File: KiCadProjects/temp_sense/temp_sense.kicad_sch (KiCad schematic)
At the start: 16 parts, among them J1 Screw_Terminal_01x02, J2 Conn_01x03_Pin, J3 Conn_01x02_Pin, U1 ADS1115IDGS, U2 INA827AIDGKR

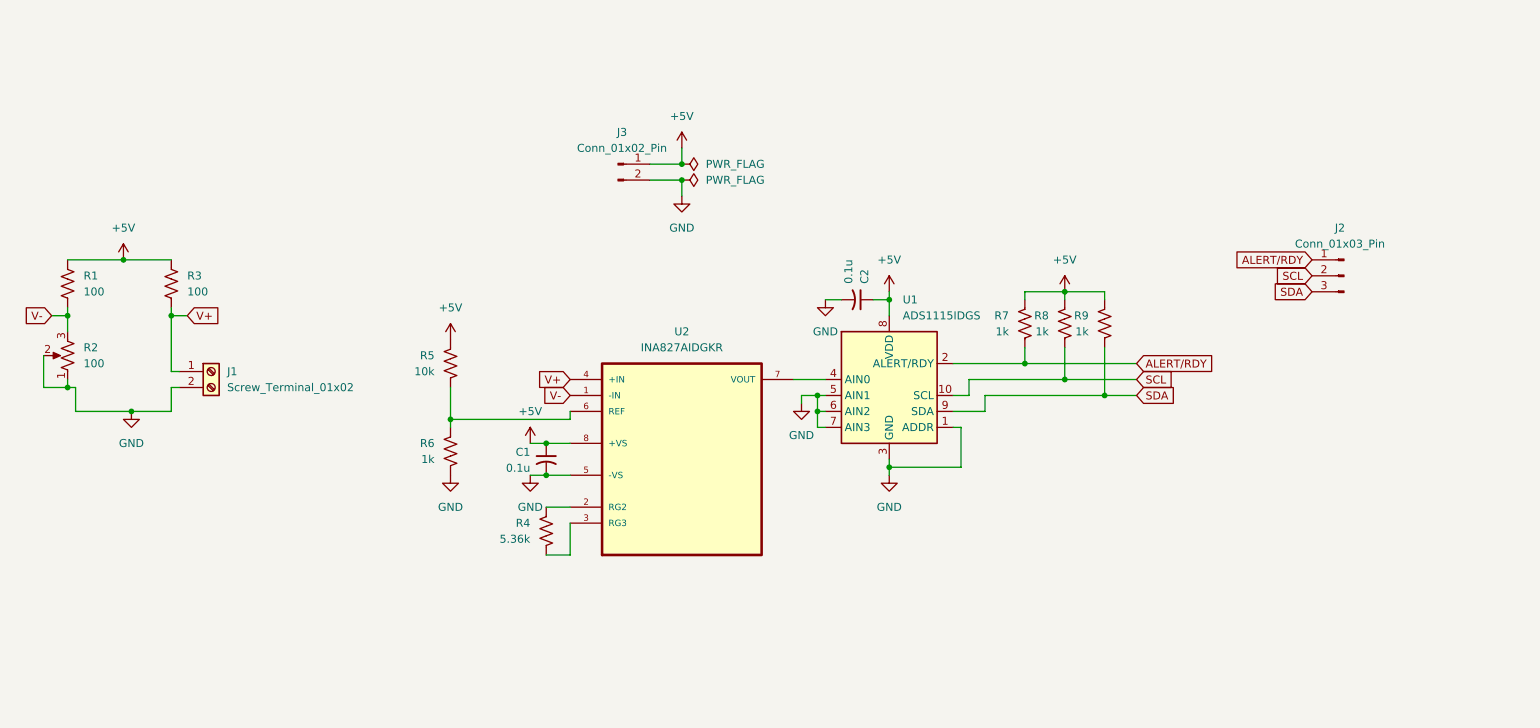
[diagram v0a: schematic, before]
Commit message: updates to temp circuit
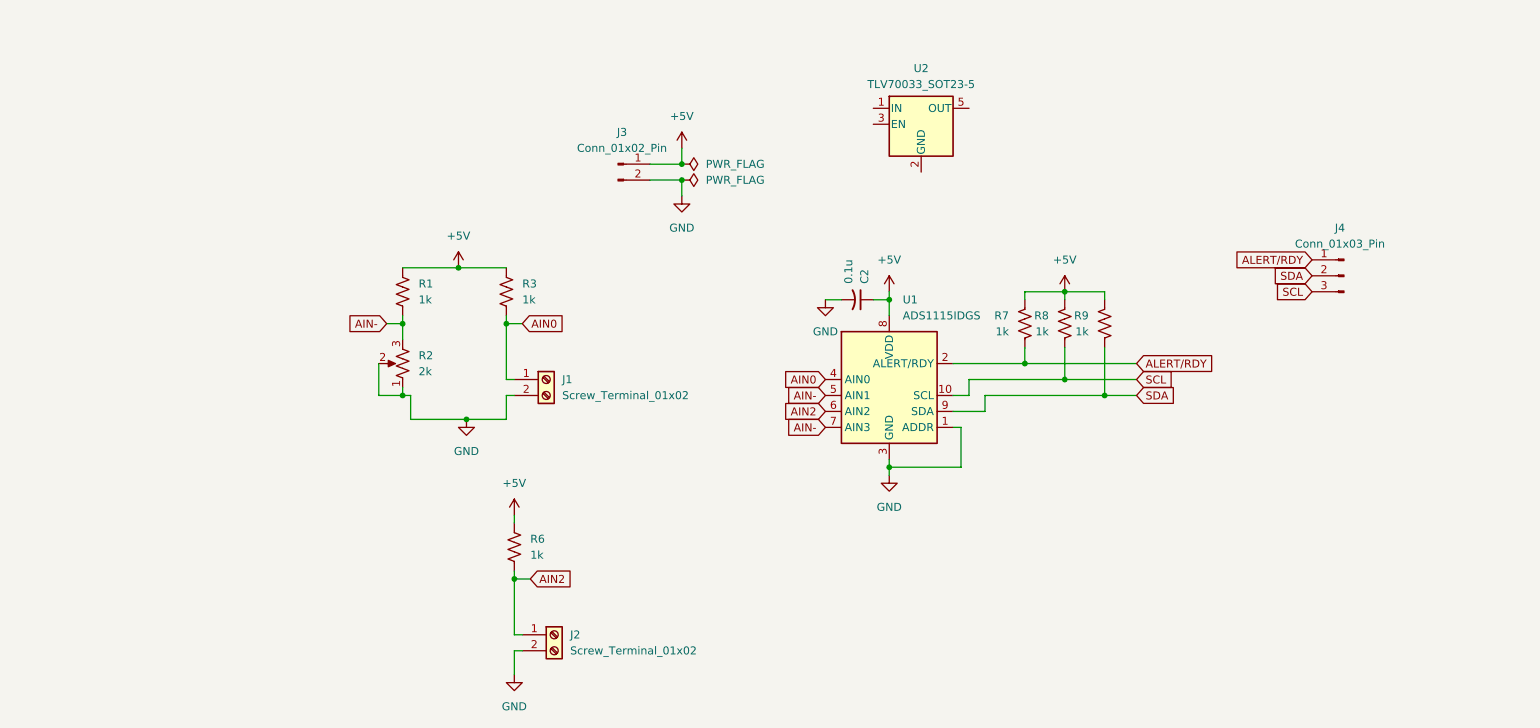
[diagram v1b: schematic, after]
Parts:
- removed C1: 0.1u, Capacitor_SMD:C_0201_0603Metric_Pad0.64x0.40mm_HandSolder, symbol Device:C_Small_US
- removed R4: 5.36k, Resistor_SMD:R_0201_0603Metric_Pad0.64x0.40mm_HandSolder, symbol Device:R_US
- removed R5: 10k, Resistor_SMD:R_0201_0603Metric_Pad0.64x0.40mm_HandSolder, symbol Device:R_US
- removed U2: INA827AIDGKR, 0_project:SOP65P490X110-8N, symbol 0_project:INA827AIDGKR
- added J2: Screw_Terminal_01x02, TerminalBlock_TE-Connectivity:TerminalBlock_TE_282834-2_1x02_P2.54mm_Horizontal, symbol Connector:Screw_Terminal_01x02
- added U2: TLV70033_SOT23-5, Package_TO_SOT_SMD:SOT-23-5, symbol Regulator_Linear:TLV70033_SOT23-5
- R1, R3: value 100 -> 1k; LCSC C105588 -> C22548; Link https://www.lcsc.com/product-detail/C105588.html -> https://www.lcsc.com/product-detail/C22548.html
- R2: value 100 -> 2k; footprint Potentiometer_THT:Potentiometer_Bourns_3386F_Vertical -> 0_project:POT_PV36W_MUR; Link https://www.digikey.com/en/products/detail/bourns-inc/3386F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 -> https://www.digikey.com/en/products/detail/bourns-inc/PV36W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; Part No. 3386F-101LF-ND -> 118-PV36W202C01B00-ND
- renumbered J2 to J4
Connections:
- net V+ is gone; now on net AIN0: J1.1 (Pin_1), R3.2
- net +5V: now also R6.1
- net GND: now also J2.2 (Pin_2); no longer R6.2, U1.5 (AIN1), U1.6 (AIN2), U1.7 (AIN3)
- net SCL: now also J4.3 (Pin_3); no longer J4.2 (Pin_2)
- net SDA: now also J4.2 (Pin_2); no longer J4.3 (Pin_3)
- net AIN0: now reaches U1.4 (AIN0)
- net V- renamed AIN-
- net AIN-: now also U1.5 (AIN1), U1.7 (AIN3)
- new net AIN2: J2.1 (Pin_1), R6.2, U1.6 (AIN2)
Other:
- moved on the sheet: J1, R1, R2, R3

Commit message: finish evm board
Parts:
- removed J3: Conn_01x02_Pin, Connector_PinHeader_2.54mm:PinHeader_1x02_P2.54mm_Vertical, symbol Connector:Conn_01x02_Pin
- added C1, C3: 1u, Capacitor_SMD:C_0201_0603Metric_Pad0.64x0.40mm_HandSolder, symbol Device:C_Small_US
- added J3: Input Header, Connector_PinHeader_2.54mm:PinHeader_1x03_P2.54mm_Vertical, symbol Connector:Conn_01x03_Pin
- added J5: VDD Select, Connector_PinHeader_2.54mm:PinHeader_1x03_P2.54mm_Vertical, symbol Connector:Conn_01x03_Pin
- added J6: AIN1 Select, Connector_PinHeader_2.54mm:PinHeader_1x03_P2.54mm_Vertical, symbol Connector:Conn_01x03_Pin
- added J7: AIN3 Select, Connector_PinHeader_2.54mm:PinHeader_1x03_P2.54mm_Vertical, symbol Connector:Conn_01x03_Pin
- added J8: Pull-Up Jumper, Connector_PinHeader_2.54mm:PinHeader_1x02_P2.54mm_Vertical, symbol Connector:Conn_01x02_Pin
- added J9: ADDR Select, Connector_PinHeader_2.54mm:PinHeader_1x05_P2.54mm_Vertical, symbol Connector:Conn_01x05_Pin
- J1: value Screw_Terminal_01x02 -> Sensor Input 1
- J2: value Screw_Terminal_01x02 -> Sensor Input 2
- J4: value Conn_01x03_Pin -> Output Header
- U2: LCSC (none) -> C11337; Link (none) -> https://www.lcsc.com/product-detail/C11337.html?s_z=h_tlv70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
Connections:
- net +5V: now also U2.1 (IN), C1.1, J3.1 (Pin_1), J5.1 (Pin_1), J8.1 (Pin_1); no longer C2.1, R3.1, R6.1, U1.8 (VDD)
- net ALERT/RDY: now also R9.2; no longer R7.2
- net GND: now also U2.2 (GND), C1.2, C3.2, J3.3 (Pin_3), J6.3 (Pin_3), J7.3 (Pin_3), J9.2 (Pin_2); no longer U1.1 (ADDR)
- net SCL: now also J4.2 (Pin_2), J9.4 (Pin_4); no longer J4.3 (Pin_3)
- net SDA: now also J4.3 (Pin_3), R7.2, J9.5 (Pin_5); no longer J4.2 (Pin_2), R9.2
- net EN: now reaches U2.3 (EN)
- net EN: now also J3.2 (Pin_2)
- net +3.3V: now reaches U2.5 (OUT)
- net +3.3V: now also C3.1, J5.3 (Pin_3)
- net AIN- renamed REF
- net REF: now also J6.1 (Pin_1), J7.1 (Pin_1); no longer U1.5 (AIN1), U1.7 (AIN3)
- new net: J8.2 (Pin_2), R3.1, R6.1
- new net ADDR: J9.1 (Pin_1), U1.1 (ADDR)
- new net AIN1: J6.2 (Pin_2), U1.5 (AIN1)
- new net AIN3: J7.2 (Pin_2), U1.7 (AIN3)
- new net VDD: C2.1, J5.2 (Pin_2), J9.3 (Pin_3), U1.8 (VDD)
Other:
- note added: "3.3V LDO"
- note added: "ADC"
- note added: "ADC Input Selection"
- note added: "I2C Output"
- note added: "MCU Input"
- note added: "Reference Circuit"
- note added: "Sensor Input Circuit"
- moved on the sheet: C2, J1, J2, J4, R1, R2, R3, R6, R7, R8, R9, U1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

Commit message: temp sense rev 2
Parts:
- removed J3: Input Header, Connector_PinHeader_2.54mm:PinHeader_1x03_P2.54mm_Vertical, symbol Connector:Conn_01x03_Pin
- removed J4: Output Header, Connector_PinHeader_2.54mm:PinHeader_1x03_P2.54mm_Vertical, symbol Connector:Conn_01x03_Pin
- removed J6: AIN1 Select, Connector_PinHeader_2.54mm:PinHeader_1x03_P2.54mm_Vertical, symbol Connector:Conn_01x03_Pin
- removed J7: AIN3 Select, Connector_PinHeader_2.54mm:PinHeader_1x03_P2.54mm_Vertical, symbol Connector:Conn_01x03_Pin
- removed J9: ADDR Select, Connector_PinHeader_2.54mm:PinHeader_1x05_P2.54mm_Vertical, symbol Connector:Conn_01x05_Pin
- removed R1: 1k, Resistor_SMD:R_0201_0603Metric_Pad0.64x0.40mm_HandSolder, symbol Device:R_US
- removed R2: 2k, 0_project:POT_PV36W_MUR, symbol Device:R_Potentiometer_US
- added D1, D2: LED, LED_SMD:LED_0603_1608Metric, symbol Device:LED
- added J5, J6: Conn_01x06_Pin, Connector_PinHeader_2.54mm:PinHeader_1x06_P2.54mm_Vertical, symbol Connector:Conn_01x06_Pin
- added R3, R4: 1k, Resistor_SMD:R_0603_1608Metric_Pad0.98x0.95mm_HandSolder, symbol Device:R_US
- C1, C2, C3: footprint Capacitor_SMD:C_0201_0603Metric_Pad0.64x0.40mm_HandSolder -> Capacitor_SMD:C_0603_1608Metric_Pad1.08x0.95mm_HandSolder
- R1: renamed from R3; footprint Resistor_SMD:R_0201_0603Metric_Pad0.64x0.40mm_HandSolder -> Resistor_SMD:R_0603_1608Metric_Pad0.98x0.95mm_HandSolder
- R2: renamed from R6; footprint Resistor_SMD:R_0201_0603Metric_Pad0.64x0.40mm_HandSolder -> Resistor_SMD:R_0603_1608Metric_Pad0.98x0.95mm_HandSolder
- R5: renamed from R7; footprint Resistor_SMD:R_0201_0603Metric_Pad0.64x0.40mm_HandSolder -> Resistor_SMD:R_0603_1608Metric_Pad0.98x0.95mm_HandSolder
- R6: renamed from R8; footprint Resistor_SMD:R_0201_0603Metric_Pad0.64x0.40mm_HandSolder -> Resistor_SMD:R_0603_1608Metric_Pad0.98x0.95mm_HandSolder
- R7: renamed from R9; footprint Resistor_SMD:R_0201_0603Metric_Pad0.64x0.40mm_HandSolder -> Resistor_SMD:R_0603_1608Metric_Pad0.98x0.95mm_HandSolder
- renumbered J8 to J3, J5 to J4
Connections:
- net +3.3V: now also D2.2 (A), J6.1 (Pin_1)
- net +5V: now also D1.2 (A), J5.1 (Pin_1)
- net ADDR: now also J5.2 (Pin_2)
- net AIN0: now also J5.5 (Pin_5)
- net AIN1: now also J5.6 (Pin_6)
- net AIN2: now also J6.6 (Pin_6)
- net AIN3: now also J6.5 (Pin_5)
- net ALERT/RDY: now also J5.3 (Pin_3)
- net EN: now also J6.2 (Pin_2)
- net GND: now also J5.4 (Pin_4), R3.2, R4.2
- net SCL: now also R5.2, J6.3 (Pin_3); no longer R6.2
- net SDA: now also R6.2, J6.4 (Pin_4); no longer R5.2
- new net: D1.1 (K), R3.1
- new net: D2.1 (K), R4.1
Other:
- note added: "I2C Pull-up"
- note added: "Power LEDs"
- note removed: "ADC Input Selection"
- note removed: "I2C Output"
- note removed: "MCU Input"
- note removed: "Reference Circuit"
- moved on the sheet: C2, J1, J2, J3, J4, R1, R2, U1
